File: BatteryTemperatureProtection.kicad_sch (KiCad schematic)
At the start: 8 parts, among them Q1 SIRA99DP-T1-GE3, Q2 IRLML2803

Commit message: Idk some changes
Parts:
- D3: DIS Digi-Key -> (none); DPN 511-1584-1-ND -> (none); MFR Rohm -> (none); MPN SML-E12M8WT86 -> C2909774
- Q1: MPN (none) -> C3289459
- Q2: MPN (none) -> C2590
- R10: DIS Digi-Key -> (none); DPN A129693CT-ND -> (none); MFR TE -> (none); MPN CRGCQ0603F2K7 -> C2479067
- R7, R9: DIS Digi-Key -> (none); DPN 311-10.0KHRCT-ND -> (none); MFR Yageo -> (none); MPN RC0603FR-0710KL -> C2479067
- R8: DIS Digi-Key -> (none); DPN A129693CT-ND -> (none); MFR TE -> (none); MPN CRGCQ0603F2K7 -> C2484712
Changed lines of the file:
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@@
 			)
 		)
-		(property "DIS" "Digi-Key"
-			(at 119.38 105.41 0)
-			(effects
-				(font
-					(size 1.27 1.27)
-				)
-				(justify left bottom)
-				(hide yes)
-			)
-		)
-		(property "DPN" "A129693CT-ND"
-			(at 119.38 105.41 0)
-			(effects
-				(font
-					(size 1.27 1.27)
-				)
-				(justify left bottom)
-				(hide yes)
-			)
-		)
-		(property "MFR" "TE"
-			(at 119.38 105.41 0)
-			(effects
-				(font
-					(size 1.27 1.27)
-				)
-				(justify left bottom)
-				(hide yes)
-			)
-		)
-		(property "MPN" "CRGCQ0603F2K7"
-			(at 119.38 105.41 0)
-			(effects
-				(font
-					(size 1.27 1.27)
-				)
-				(justify left bottom)
+		(property "MPN" "C2484712"
+			(at 119.38 105.41 90)
+			(effects
+				(font
+					(size 1.27 1.27)
+				)
 				(hide yes)
 			)
@@
 			)
 		)
-		(property "DIS" "Digi-Key"
+		(property "MPN" "C2479067"
 			(at 111.76 111.76 0)
 			(effects
@@
 					(size 1.27 1.27)
 				)
-				(justify left bottom)
-				(hide yes)
-			)
-		)
-		(property "DPN" "311-10.0KHRCT-ND"
-			(at 111.76 111.76 0)
-			(effects
-				(font
-					(size 1.27 1.27)
-				)
-				(justify left bottom)
-				(hide yes)
-			)
-		)
-		(property "MFR" "Yageo"
-			(at 111.76 111.76 0)
-			(effects
-				(font
-					(size 1.27 1.27)
-				)
-				(justify left bottom)
-				(hide yes)
-			)
-		)
-		(property "MPN" "RC0603FR-0710KL"
-			(at 111.76 111.76 0)
-			(effects
-				(font
-					(size 1.27 1.27)
-				)
-				(justify left bottom)
 				(hide yes)
 			)
@@
 		(property "Description" ""
 			(at 130.81 105.41 0)
+			(effects
+				(font
+					(size 1.27 1.27)
+				)
+				(hide yes)
+			)
+		)
+		(property "MPN" "C2590"
+			(at 133.35 105.41 0)
 			(effects
 				(font
@@
 			)
 		)
+		(property "MPN" "C3289459"
+			(at 147.32 90.17 90)
+			(effects
+				(font
+					(size 1.27 1.27)
+				)
+				(hide yes)
+			)
+		)
 		(pin "5"
 		)
@@
 			)
 		)
-		(property "DIS" "Digi-Key"
+		(property "MPN" "C2479067"
 			(at 162.56 95.25 0)
 			(effects
@@
 					(size 1.27 1.27)
 				)
-				(justify left bottom)
-				(hide yes)
-			)
-		)
-		(property "DPN" "A129693CT-ND"
-			(at 162.56 95.25 0)
-			(effects
-				(font
-					(size 1.27 1.27)
-				)
-				(justify left bottom)
-				(hide yes)
-			)
-		)
-		(property "MFR" "TE"
-			(at 162.56 95.25 0)
-			(effects
-				(font
-					(size 1.27 1.27)
-				)
-				(justify left bottom)
-				(hide yes)
-			)
-		)
-		(property "MPN" "CRGCQ0603F2K7"
-			(at 162.56 95.25 0)
-			(effects
-				(font
-					(size 1.27 1.27)
-				)
-				(justify left bottom)
 				(hide yes)
 			)
@@
 			)
 		)
-		(property "DIS" "Digi-Key"
+		(property "MPN" "C2479067"
 			(at 133.35 92.71 0)
 			(effects
@@
 					(size 1.27 1.27)
 				)
-				(justify left bottom)
-				(hide yes)
-			)
-		)
-		(property "DPN" "311-10.0KHRCT-ND"
-			(at 133.35 92.71 0)
-			(effects
-				(font
-					(size 1.27 1.27)
-				)
-				(justify left bottom)
-				(hide yes)
-			)
-		)
-		(property "MFR" "Yageo"
-			(at 133.35 92.71 0)
-			(effects
-				(font
-					(size 1.27 1.27)
-				)
-				(justify left bottom)
-				(hide yes)
-			)
-		)
-		(property "MPN" "RC0603FR-0710KL"
-			(at 133.35 92.71 0)
-			(effects
-				(font
-					(size 1.27 1.27)
-				)
-				(justify left bottom)
 				(hide yes)
 			)
@@
 			)
 		)
-		(property "DIS" "Digi-Key"
+		(property "MPN" "C2909774"
 			(at 162.56 104.14 0)
 			(effects
@@
 				(hide yes)
 			)
-		)
-		(property "DPN" "511-1584-1-ND"
-			(at 162.56 104.14 0)
-			(effects
-				(font
-					(size 1.27 1.27)
-				)
-				(justify left bottom)
-				(hide yes)
-			)
-		)
-		(property "MFR" "Rohm"
-			(at 162.56 104.14 0)
-			(effects
-				(font
-					(size 1.27 1.27)
-				)
-				(justify left bottom)
-				(hide yes)
-			)
-		)
-		(property "MPN" "SML-E12M8WT86"
-			(at 162.56 104.14 0)
-			(effects
-				(font
-					(size 1.27 1.27)
-				)
-				(justify left bottom)
-				(hide yes)
-			)
-		)
-		(property "Sim.Pin" "1=K 2=A"
-			(at 162.56 104.14 0)
-			(effects
-				(font
-					(size 1.27 1.27)
-				)
-				(hide yes)
-			)

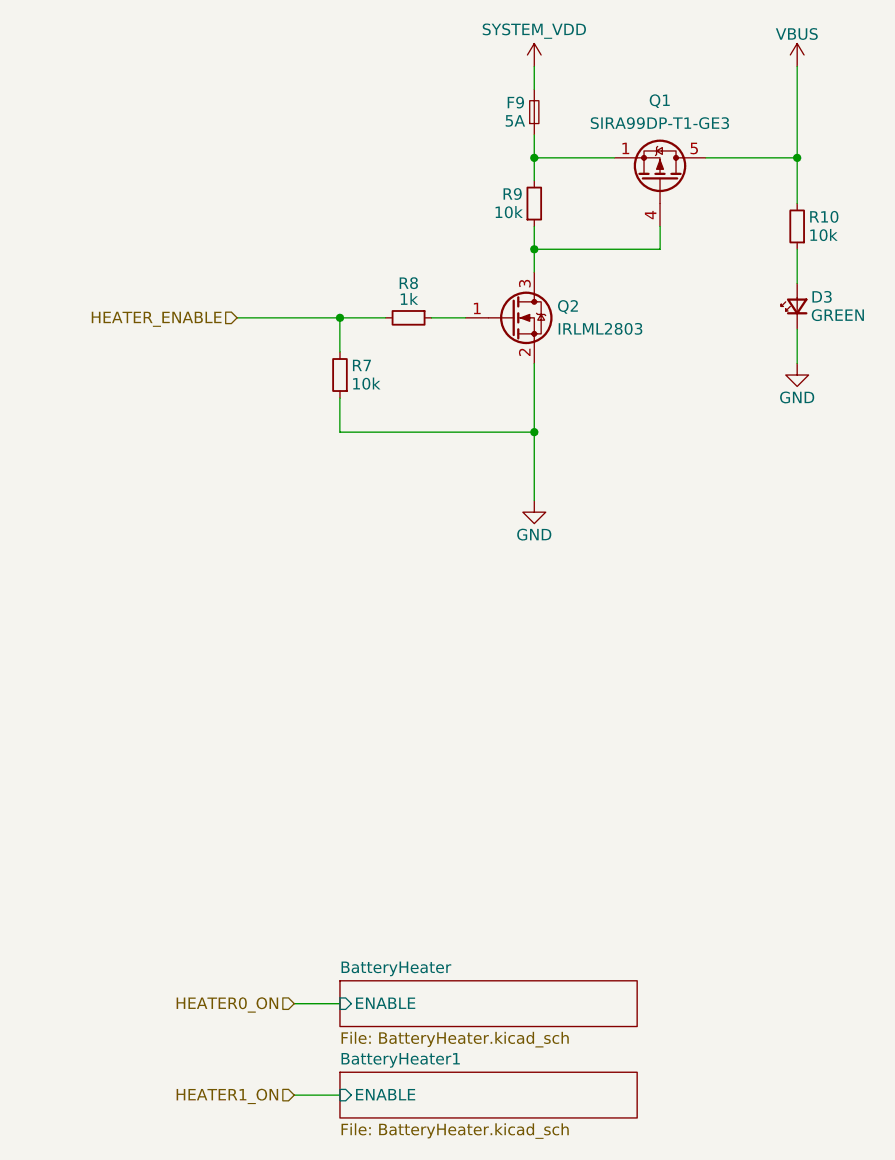
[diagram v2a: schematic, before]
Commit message: v3.2 Updates
Added 0ohm bypass. Opto-isolated heater enables
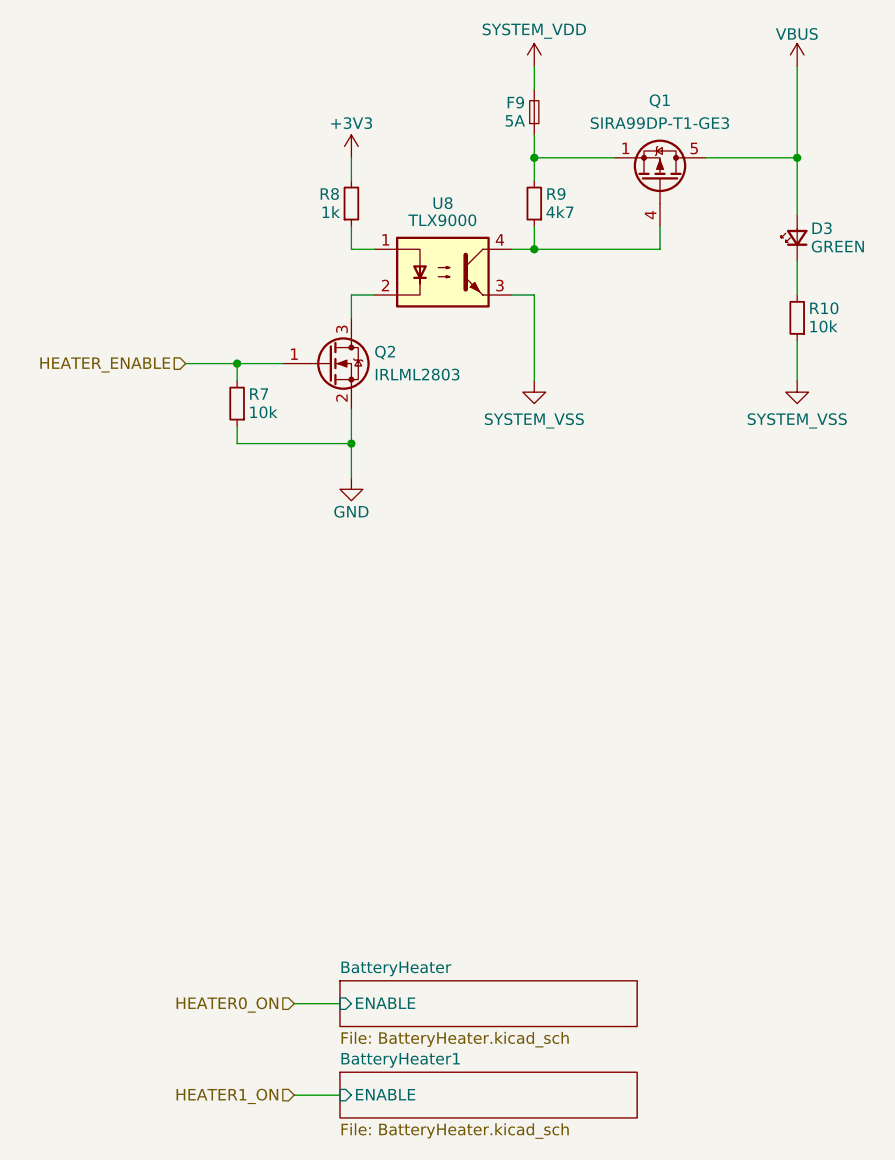
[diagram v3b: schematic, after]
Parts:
- added U8: TLX9000, Package_SO:SOIC-4_4.55x2.6mm_P1.27mm, symbol Isolator:Optocoupler_DC_PhotoNPN_AKEC
- R8: MPN C2484712 -> C2479067
- R9: value 10k -> 4k7
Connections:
- net GND: no longer D3.1 (K)
- net HEATER_ENABLE: now also Q2.1 (G); no longer R8.2
- net VBUS: now also D3.2 (A); no longer R10.2
- net at R8.1: now also U8.1; no longer Q2.1 (G)
- net at Q1.4 (G), R9.1: now also U8.4; no longer Q2.3 (D)
- net SYSTEM_VSS: now reaches R10.1
- net SYSTEM_VSS: now also U8.3; no longer D3.2 (A)
- new net: Q2.3 (D), U8.2
- new net: D3.1 (K), R10.2
- new net +3V3: R8.2
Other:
- moved on the sheet: D3, R10, R7, R9
